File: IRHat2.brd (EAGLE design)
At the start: 64.9 x 29.8 mm, 25 parts, among them T2 2N2907, T3 2N2907

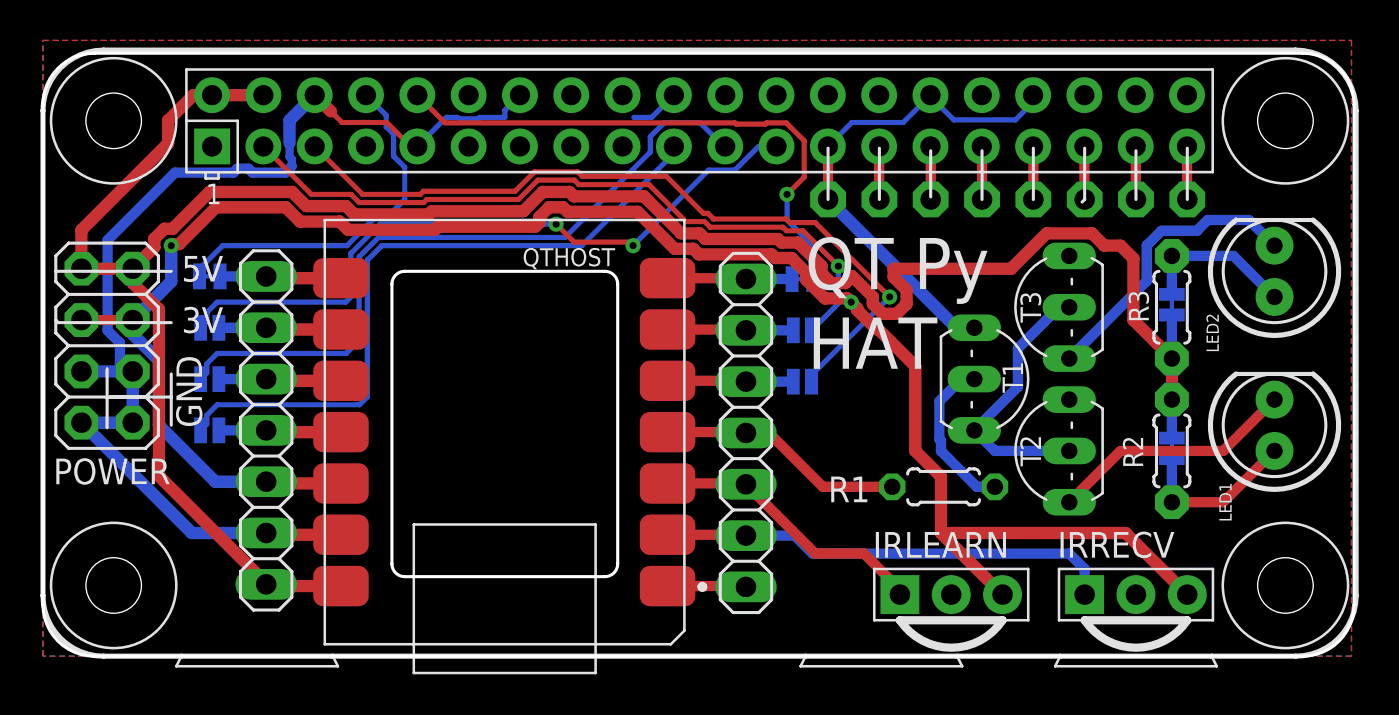
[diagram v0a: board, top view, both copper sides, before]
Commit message: tweaks and warning fixes
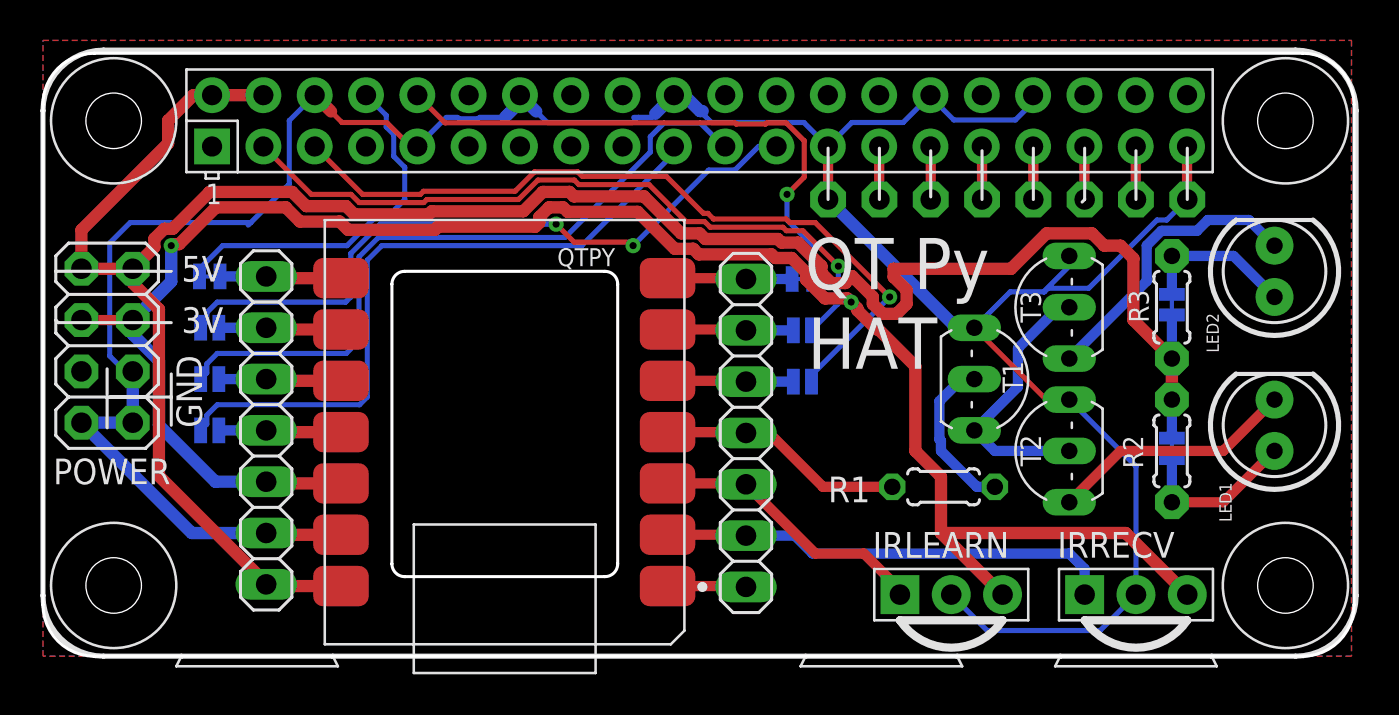
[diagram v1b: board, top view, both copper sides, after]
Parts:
- renumbered QTHOST to QTPY
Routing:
- net GND: track 87.3 -> 143.4 mm
